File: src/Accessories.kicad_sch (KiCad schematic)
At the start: 64 parts, among them J26 Banana, J28 Banana, J29 Banana, J30 Banana, J31 Banana, J32 MiniFit_2x04_F, J33 Banana, J35 Banana, J36 Banana, J38 Conn_01x01, J39 Conn_01x01, J40 battery sensor, J41 Control button, J42 Battery Meter, J43 Conn_01x01, J44 Conn_01x01, J63 Conn_01x01, J74 Conn_01x01, J75 Conn_01x01, J76 Conn_01x01, J77 Conn_01x01, J78 Conn_01x01, Q2 2N7002, Q2 AO3413, Q6 AO3413, SW5 SW_Push, SW6 SW_Push

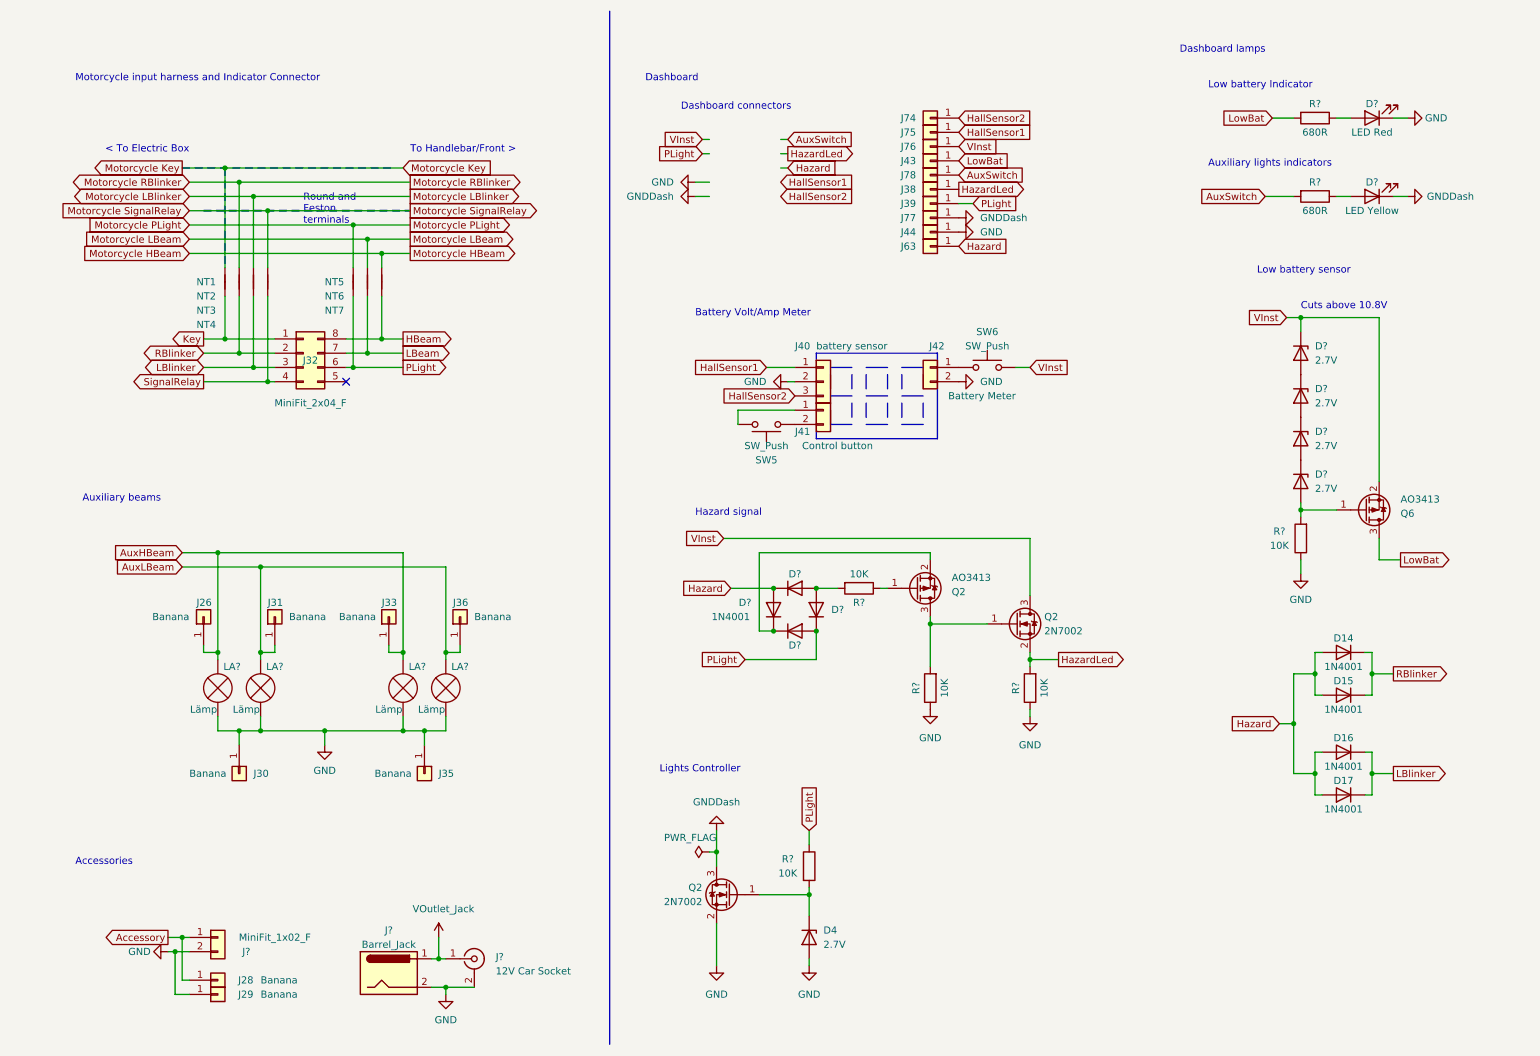
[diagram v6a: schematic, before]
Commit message: Simplify circuit diagram. Remove unecessary features
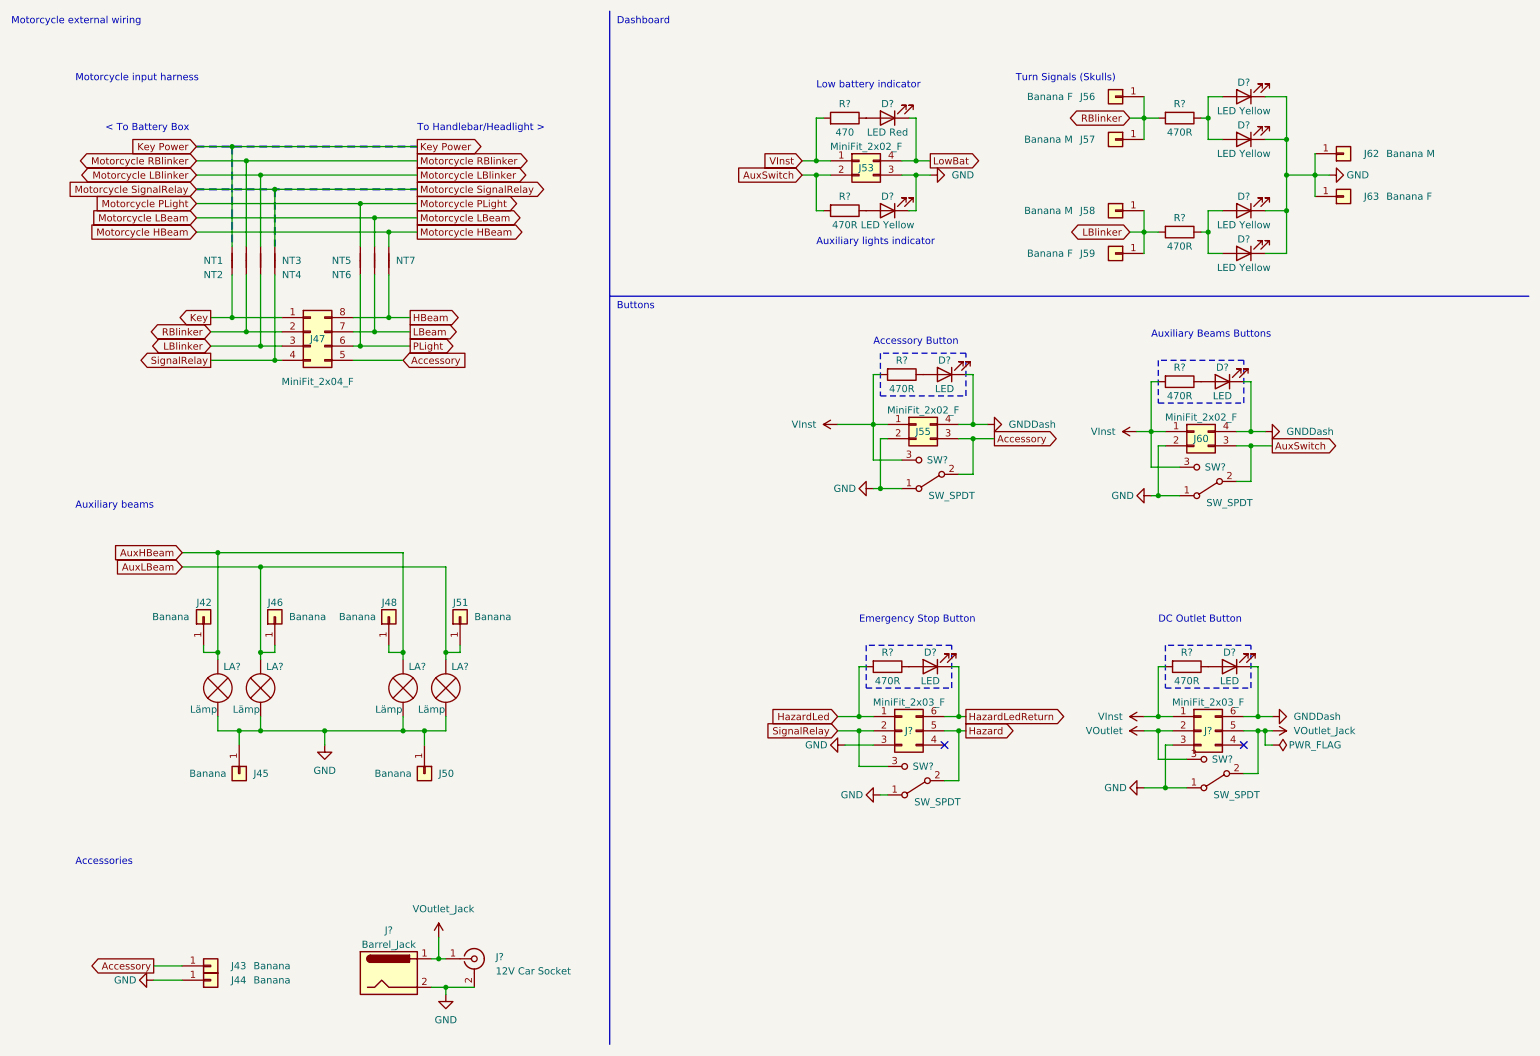
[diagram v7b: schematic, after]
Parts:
- removed D14, D15, D16, D17, D? (x4): 1N4001, Diode_THT:D_DO-41_SOD81_P10.16mm_Horizontal, symbol Diode:1N4001
- removed D4, D? (x4): 2.7V, Diode_THT:D_DO-35_SOD27_P7.62mm_Horizontal, symbol Diode:BZV55C2V7
- removed D?: LED Red, LED_THT:LED_D5.0mm, symbol Device:LED
- removed J38, J39, J43, J44, J74, J75, J76, J77, J78: Conn_01x01, TestPoint:TestPoint_THTPad_D2.5mm_Drill1.2mm, symbol Connector_Generic:Conn_01x01
- removed J40: battery sensor, symbol Connector_Generic:Conn_01x03
- removed J41: Control button, symbol Connector_Generic:Conn_01x02
- removed J42: Battery Meter, symbol Connector_Generic:Conn_01x02
- removed J?: MiniFit_1x02_F, symbol Connector_Generic:Conn_01x02
- removed Q2, Q6: AO3413, Package_TO_SOT_SMD:SOT-23, symbol Transistor_FET:AO3401A
- removed Q2 (x2): 2N7002, Package_TO_SOT_SMD:SOT-23, symbol Transistor_FET:2N7002
- removed R? (x5): 10K, Resistor_SMD:R_1206_3216Metric_Pad1.30x1.75mm_HandSolder, symbol Device:R
- removed R?: 680R, Resistor_THT:R_Axial_DIN0204_L3.6mm_D1.6mm_P5.08mm_Horizontal, symbol Device:R
- removed SW5, SW6: SW_Push, symbol Switch:SW_Push
- added D? (x4): LED Yellow, LED_THT:LED_D5.0mm, symbol Device:LED
- added D? (x4): LED, symbol Device:LED
- added D?: LED Red, LED_THT:LED_D5.0mm, symbol Device:LED
- added J53, J55, J60: MiniFit_2x02_F, symbol Connector_Generic:Conn_02x02_Counter_Clockwise
- added J56, J59: Banana F, symbol Connector_Generic:Conn_01x01
- added J57, J58, J62: Banana M, symbol Connector_Generic:Conn_01x01
- added J? (x2): MiniFit_2x03_F, symbol Connector_Generic:Conn_02x03_Counter_Clockwise
- added R? (x2): 470R, Resistor_THT:R_Axial_DIN0204_L3.6mm_D1.6mm_P5.08mm_Horizontal, symbol Device:R
- added R? (x4): 470R, symbol Device:R
- added R?: 470, Resistor_THT:R_Axial_DIN0204_L3.6mm_D1.6mm_P5.08mm_Horizontal, symbol Device:R
- added SW? (x4): SW_SPDT, symbol Switch:SW_SPDT
- J63: value Conn_01x01 -> Banana F; footprint TestPoint:TestPoint_THTPad_D2.5mm_Drill1.2mm -> (none)
- R?: value 680R -> 470R
- renumbered J26 to J42, J28 to J43, J29 to J44, J30 to J45, J31 to J46, J32 to J47, J33 to J48, J35 to J50, J36 to J51
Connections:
- net Accessory: now also J47.5 (Pin_5), J55.3 (Pin_3), SW?.2 (B)
- net AuxSwitch: now also J53.2 (Pin_2), J60.3 (Pin_3), SW?.2 (B)
- net GND: now also D?.1 (K), J63.1 (Pin_1), D?.1 (K), D?.1 (K), D?.1 (K), D?.1 (K), J53.3 (Pin_3), J55.2 (Pin_2), J60.2 (Pin_2), J62.1 (Pin_1), J?.3 (Pin_3), J?.3 (Pin_3), SW?.1 (A), SW?.1 (A), SW?.1 (A), SW?.1 (A)
- net GNDDash: now also D?.1 (K), D?.1 (K), D?.1 (K), J55.4 (Pin_4), J60.4 (Pin_4), J?.6 (Pin_6); no longer D?.1 (K)
- net Hazard: now also J?.5 (Pin_5), SW?.2 (B); no longer J63.1 (Pin_1)
- net HazardLed: now also J?.1 (Pin_1), R?.2
- net LBlinker: now also J58.1 (Pin_1), J59.1 (Pin_1), R?.2
- net LowBat: now also D?.1 (K), J53.4 (Pin_4)
- net RBlinker: now also J56.1 (Pin_1), J57.1 (Pin_1), R?.2
- net SignalRelay: now also J?.2 (Pin_2), SW?.3 (C)
- net VInst: now also J53.1 (Pin_1), J55.1 (Pin_1), J60.1 (Pin_1), J?.1 (Pin_1), R?.2, R?.2, R?.2, R?.2, SW?.3 (C), SW?.3 (C)
- net VOutlet_Jack: now also J?.5 (Pin_5), SW?.2 (B)
- net Motorcycle Key renamed Key Power
- new net: D?.2 (A), D?.2 (A), R?.1 (x2)
- new net: D?.2 (A), R?.1 (x5)
- new net HazardLedReturn: D?.1 (K), J?.6 (Pin_6)
- new net VOutlet: J?.2 (Pin_2), SW?.3 (C)
- no-connect marks 1 -> 2
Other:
- note added: "< To Battery Box"
- note added: "Accessory Button"
- note added: "Auxiliary Beams Buttons"
- note added: "Auxiliary lights indicator"
- note added: "Buttons"
- note added: "DC Outlet Button"
- note added: "Emergency Stop Button"
- note added: "Low battery indicator"
- note added: "Motorcycle external wiring"
- note added: "Motorcycle input harness"
- note added: "To Handlebar/Headlight >"
- note added: "Turn Signals (Skulls)"
- note removed: "< To Electric Box"
- note removed: "Auxiliary lights indicators"
- note removed: "Battery Volt/Amp Meter"
- note removed: "Cuts above 10.8V"
- note removed: "Dashboard connectors"
- note removed: "Dashboard lamps"
- note removed: "Hazard signal"
- note removed: "Lights Controller"
- note removed: "Low battery Indicator"
- note removed: "Low battery sensor"
- note removed: "Motorcycle input harness and Indicator Connector"
- note removed: "Round and Feston terminals"
- note removed: "To Handlebar/Front >"
- moved on the sheet: D?, J43, J44, J47, NT1, NT2, NT3, NT4, NT5, NT6, NT7, R?

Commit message: Fix battery sensor
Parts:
- removed J53: MiniFit_2x02_F, symbol Connector_Generic:Conn_02x02_Counter_Clockwise
- added D27: Green, LED_THT:LED_D5.0mm, symbol Device:LED
- added D28: LED Yellow, LED_THT:LED_D5.0mm, symbol Device:LED
- added J79: MiniFit_2x03_F, symbol Connector_Generic:Conn_02x03_Counter_Clockwise
- added R18, R19: 1K, Resistor_THT:R_Axial_DIN0204_L3.6mm_D1.6mm_P5.08mm_Horizontal, symbol Device:R
- R10: renamed from R?; value 470R -> 1K
- R13, R14: renamed from R?; value 470R -> 560R
- R9: renamed from R?; value 470 -> 1K
- gave numbers to parts that had none: 26
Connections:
- net Accessory: now also J79.3 (Pin_3), R18.2
- net AuxSwitch: now also J79.2 (Pin_2)
- net GND: now also D27.1 (K), D28.1 (K), J79.4 (Pin_4)
- net LowBat: now also J79.6 (Pin_6)
- net VInst: now also J79.1 (Pin_1)
- net VOutlet_Jack: now also J79.5 (Pin_5), R19.2
- new net: D28.2 (A), R19.1
- new net: D27.2 (A), R18.1
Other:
- note added: "Auxiliary lights on indicator"
- note removed: "Auxiliary lights indicator"
- moved on the sheet: D17, D18, D19, D20, D21, D22, D23, D24, D25, D26, J54, J55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
